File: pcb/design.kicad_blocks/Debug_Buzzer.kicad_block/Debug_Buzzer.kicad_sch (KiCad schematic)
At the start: 5 parts

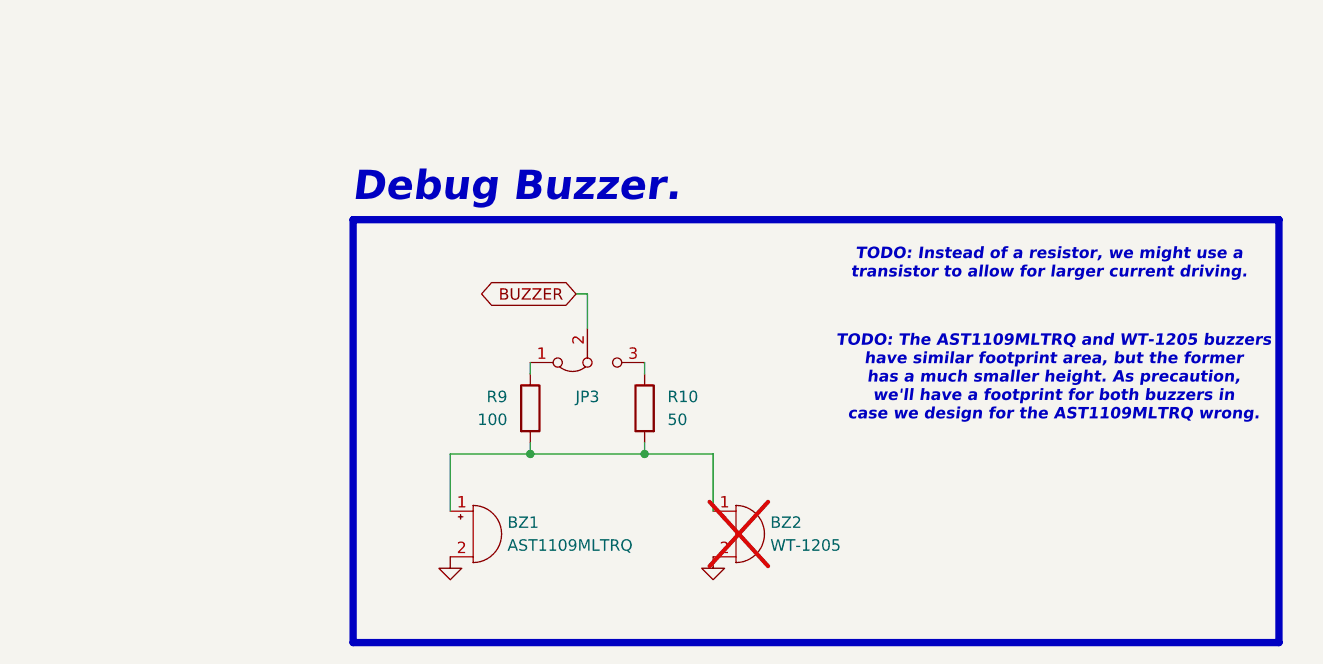
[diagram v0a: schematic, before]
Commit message: Debug buzzer connected to MCU.
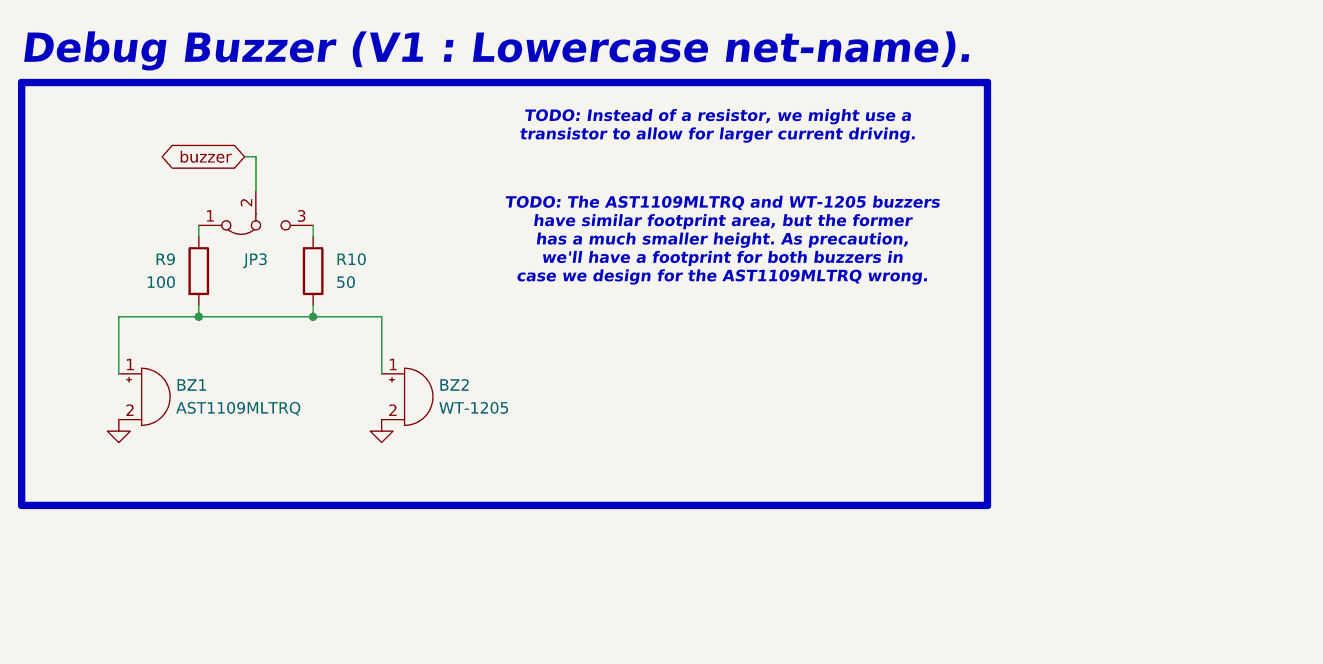
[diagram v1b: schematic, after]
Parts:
- BZ2: now fitted
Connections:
- net BUZZER renamed buzzer
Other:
- note added: "Debug Buzzer (V1 : Lowercase net-name)."
- note removed: "Debug Buzzer."
- moved on the sheet: BZ1, JP3, R10, R9

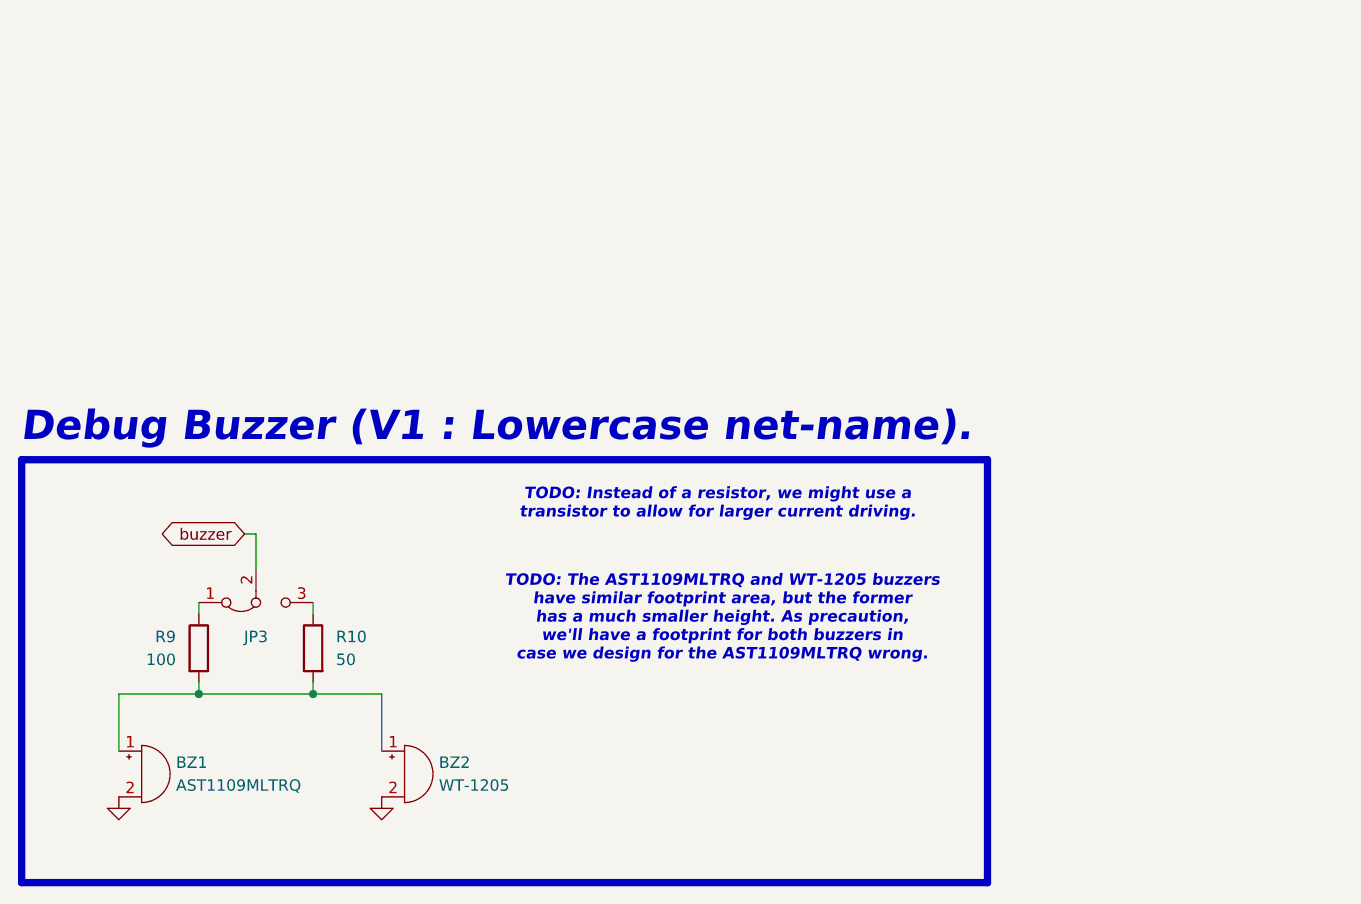
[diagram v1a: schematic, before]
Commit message: Updated design blocks of debug buzzer and debug led.
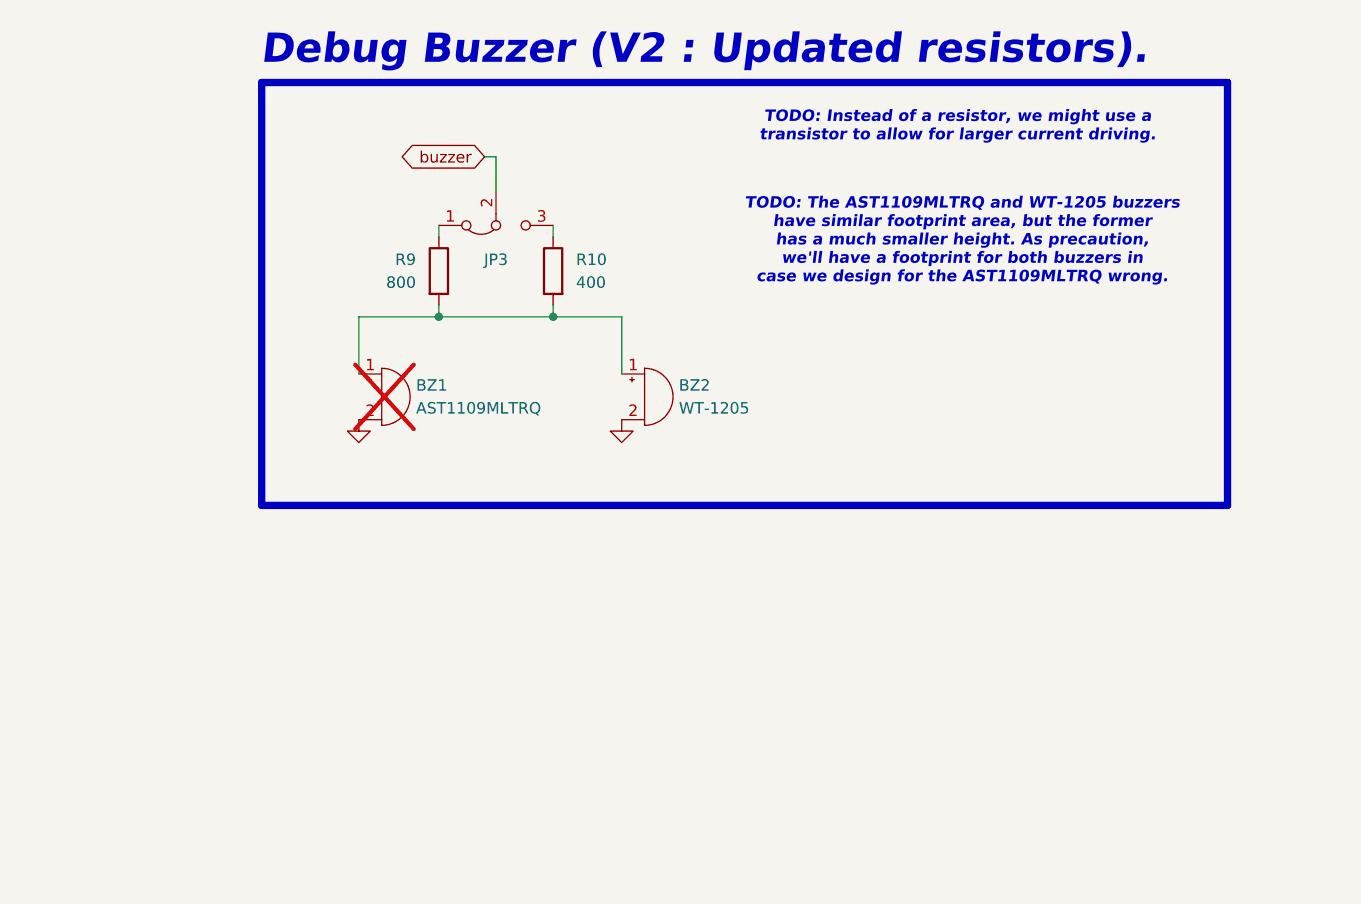
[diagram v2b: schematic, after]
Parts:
- BZ1: now not fitted
- JP3: now in the parts list
- R10: value 50 -> 400
- R9: value 100 -> 800
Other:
- note added: "Debug Buzzer (V2 : Updated resistors)."
- note removed: "Debug Buzzer (V1 : Lowercase net-name)."
- moved on the sheet: BZ2, JP3, R10, R9

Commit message: Finished routing main flight computer.
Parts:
- BZ1: now fitted
- R22: renamed from R9; value 800 -> 100
- R27: renamed from R10; value 400 -> 50
- renumbered JP3 to JP2
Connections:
- net BUZZER_ANODE: now reaches BZ1.1 (+), BZ2.1 (+), R22.2, R27.2
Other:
- note added: "Debug Buzzer (V3 : Added net-label)."
- note removed: "Debug Buzzer (V2 : Updated resistors)."
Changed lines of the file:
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@@
 		)
 	)
-	(text "Debug Buzzer (V2 : Updated resistors)."
+	(text "Debug Buzzer (V3 : Added net-label)."
 		(exclude_from_sim no)
 		(at 339.598 225.044 0)
@@
 		)
 	)
+	(label "BUZZER_ANODE"
+		(at 379.73 252.73 0)
+		(effects
+			(font
+				(size 0.635 0.635)
+			)
+			(justify left bottom)
+		)
+	)
 	(global_label "buzzer"
 		(shape bidirectional)
@@
 		(on_board yes)
 		(dnp no)
-		(property "Reference" "JP3"
+		(property "Reference" "JP2"
 			(at 365.76 246.38 0)
 			(effects
@@
 			(project "MainFlightComputer"
 				(path "/0a179c33-cb18-4019-99e7-0e00d41f97d6"
-					(reference "JP3")
+					(reference "JP2")
 					(unit 1)
 				)
@@
 		(on_board yes)
 		(dnp no)
-		(property "Reference" "R9"
+		(property "Reference" "R22"
 			(at 356.87 246.3799 0)
 			(effects
@@
 			)
 		)
-		(property "Value" "800"
+		(property "Value" "100"
 			(at 356.87 248.9199 0)
 			(effects
@@
 			(project "MainFlightComputer"
 				(path "/0a179c33-cb18-4019-99e7-0e00d41f97d6"
-					(reference "R9")
+					(reference "R22")
 					(unit 1)
 				)
@@
 		(in_bom yes)
 		(on_board yes)
-		(dnp yes)
+		(dnp no)
 		(fields_autoplaced yes)
 		(property "Reference" "BZ1"
@@
 		(on_board yes)
 		(dnp no)
-		(property "Reference" "R10"
+		(property "Reference" "R27"
 			(at 374.65 246.3799 0)
 			(effects
@@
 			)
 		)
-		(property "Value" "400"
+		(property "Value" "50"
 			(at 374.65 248.9199 0)
 			(effects
@@
 			(project "MainFlightComputer"
 				(path "/0a179c33-cb18-4019-99e7-0e00d41f97d6"
-					(reference "R10")
+					(reference "R27")
 					(unit 1)
 				)

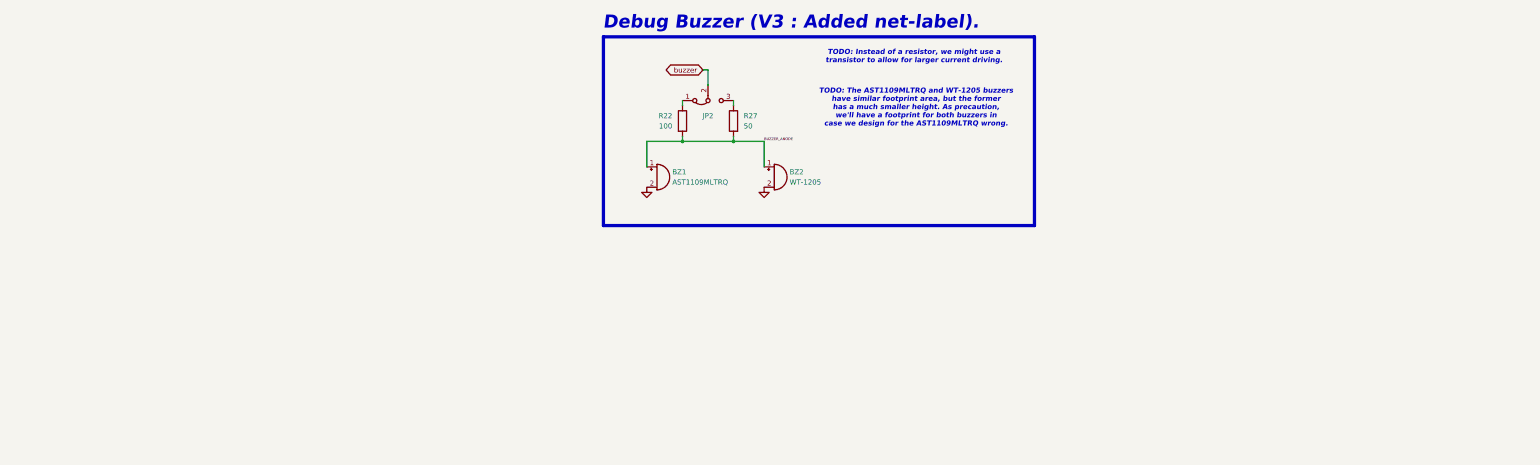
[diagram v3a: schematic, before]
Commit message: `Debug Buzzer (V4 : Transistor).` : Buzzer driven by transistor.
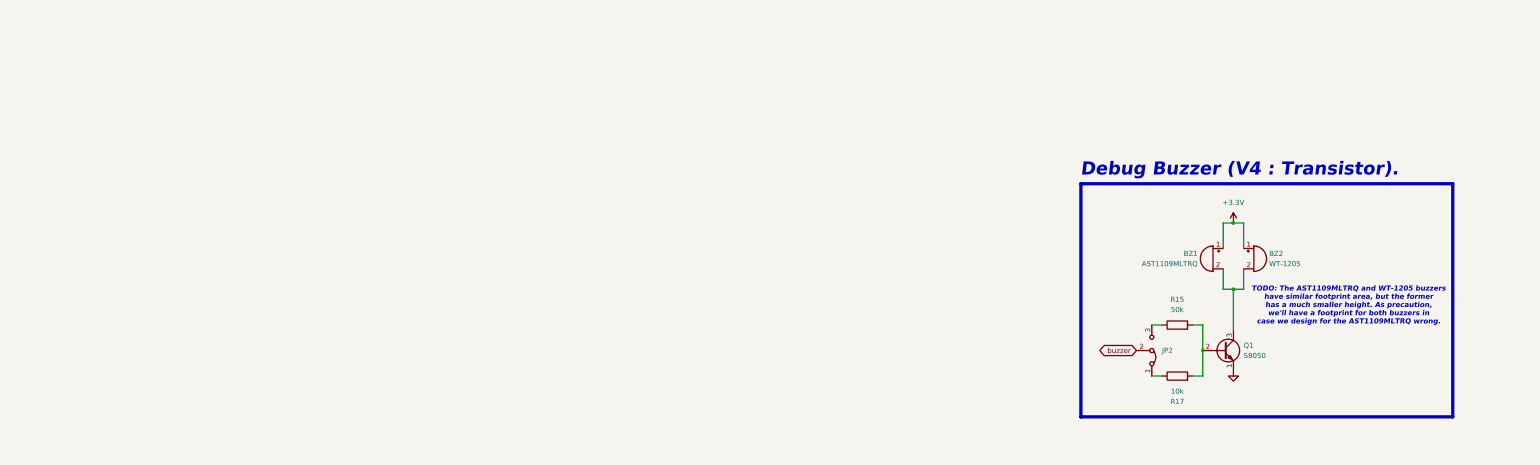
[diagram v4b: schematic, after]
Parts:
- added Q1: S8050, Package_TO_SOT_SMD:SOT-23_Handsoldering, symbol Transistor_BJT:S8050
- R15: renamed from R22; value 100 -> 50k
- R17: renamed from R27; value 50 -> 10k
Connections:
- net GND: now also Q1.1 (E); no longer BZ1.2 (-), BZ2.2 (-)
- net at JP2.1 (A): now also R17.1; no longer R15.1
- net at JP2.3 (B): now also R15.1; no longer R17.1
- net BUZZER_ANODE: no longer names the net of R15.2, R17.2
- net BUZZER_ANODE: now also Q1.2 (B); no longer BZ1.1 (+), BZ2.1 (+)
- new net: BZ1.2 (-), BZ2.2 (-), Q1.3 (C)
- new net +3.3V: BZ1.1 (+), BZ2.1 (+)
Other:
- note added: "Debug Buzzer (V4 : Transistor)."
- note removed: "Debug Buzzer (V3 : Added net-label)."
- note removed: "TODO: Instead of a resistor, we might use a transistor to allow for larger current driving."
- moved on the sheet: BZ1, BZ2, JP2, R15, R17

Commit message: `Debug Buzzer (V5 : AST only).`
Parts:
- removed BZ2: WT-1205, Buzzer_Beeper:MagneticBuzzer_ProSignal_ABT-410-RC, symbol Device:Buzzer
- Q1: footprint Package_TO_SOT_SMD:SOT-23_Handsoldering -> Package_TO_SOT_THT:TO-92_Inline
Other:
- note added: "Debug Buzzer (V5 : AST only)."
- note removed: "Debug Buzzer (V4 : Transistor)."
- note removed: "TODO: The AST1109MLTRQ and WT-1205 buzzers have similar footprint area, but the former has a much smaller height. As precaution, we'll have a footprint for both buzzers in case we design for the AST1109MLTRQ wrong."
- moved on the sheet: BZ1, JP2, Q1, R15, R17
